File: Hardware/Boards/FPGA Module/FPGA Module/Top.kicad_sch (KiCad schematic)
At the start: 2 parts

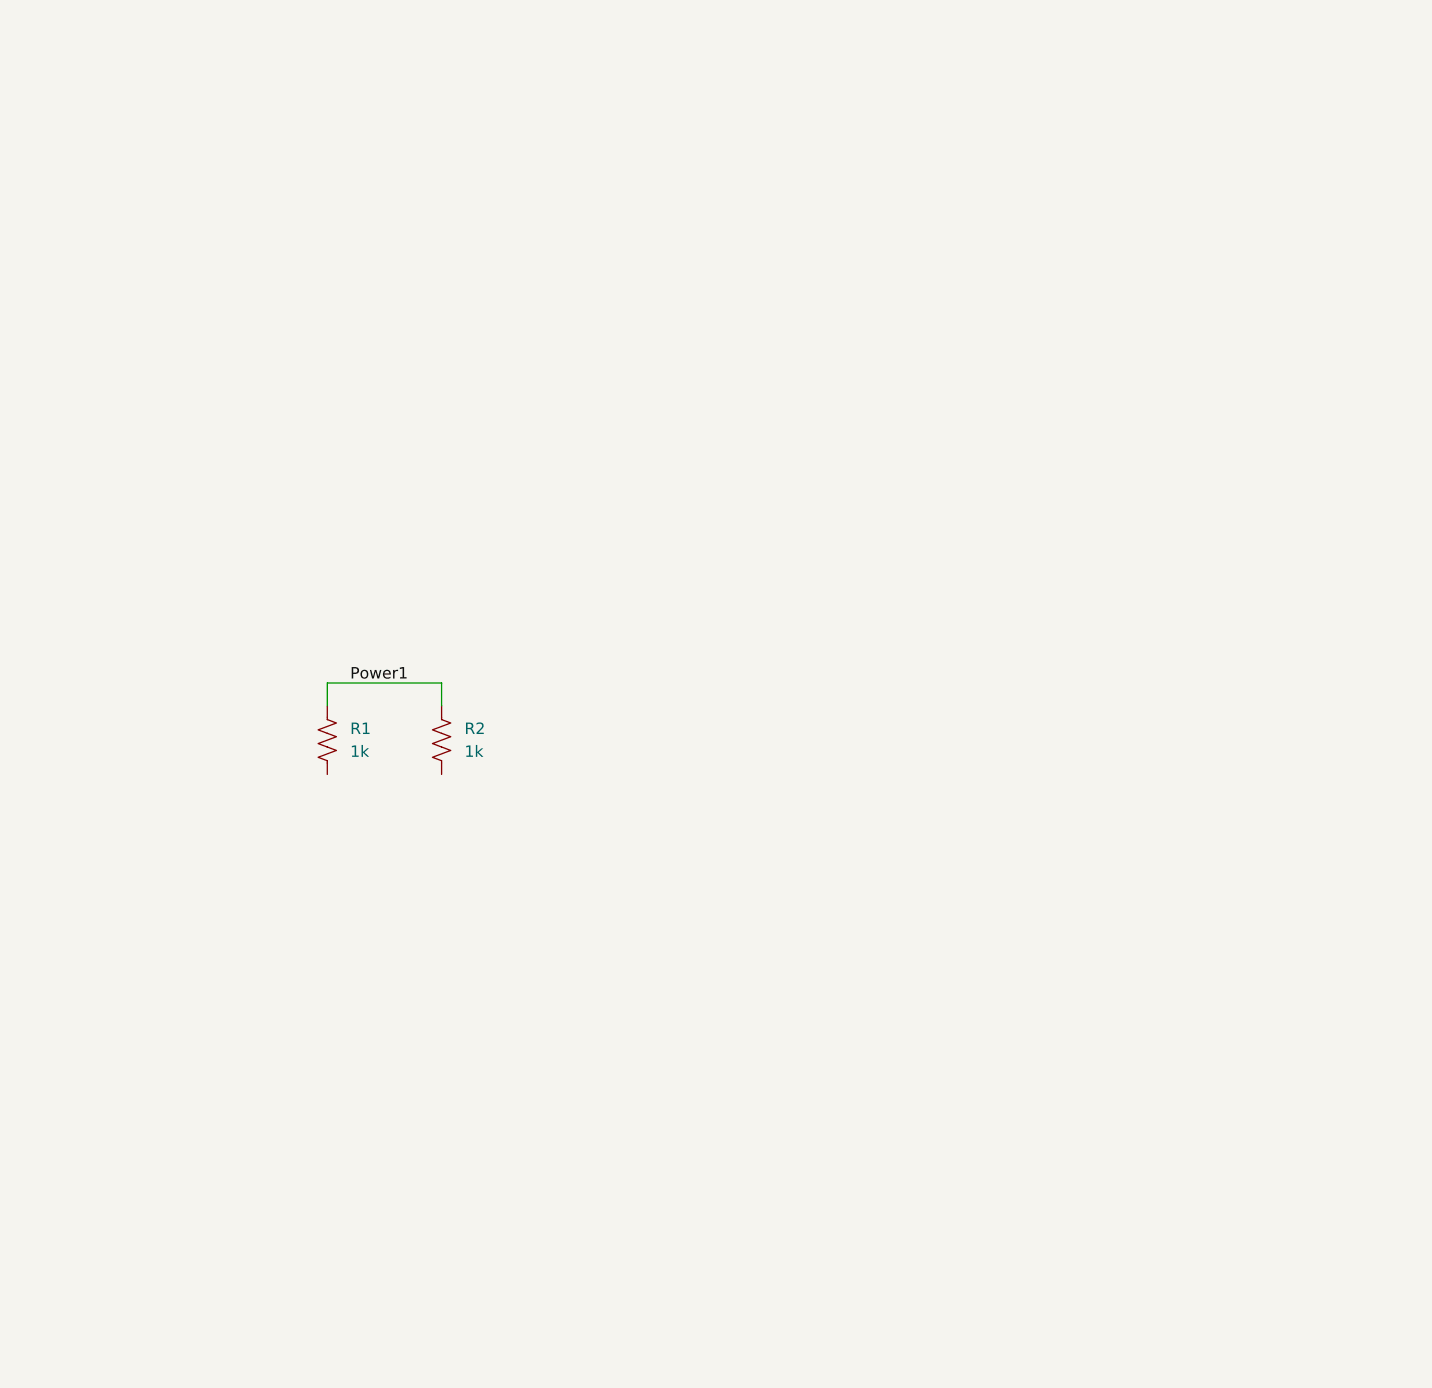
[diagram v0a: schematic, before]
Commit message: FPGA module schematic page creation
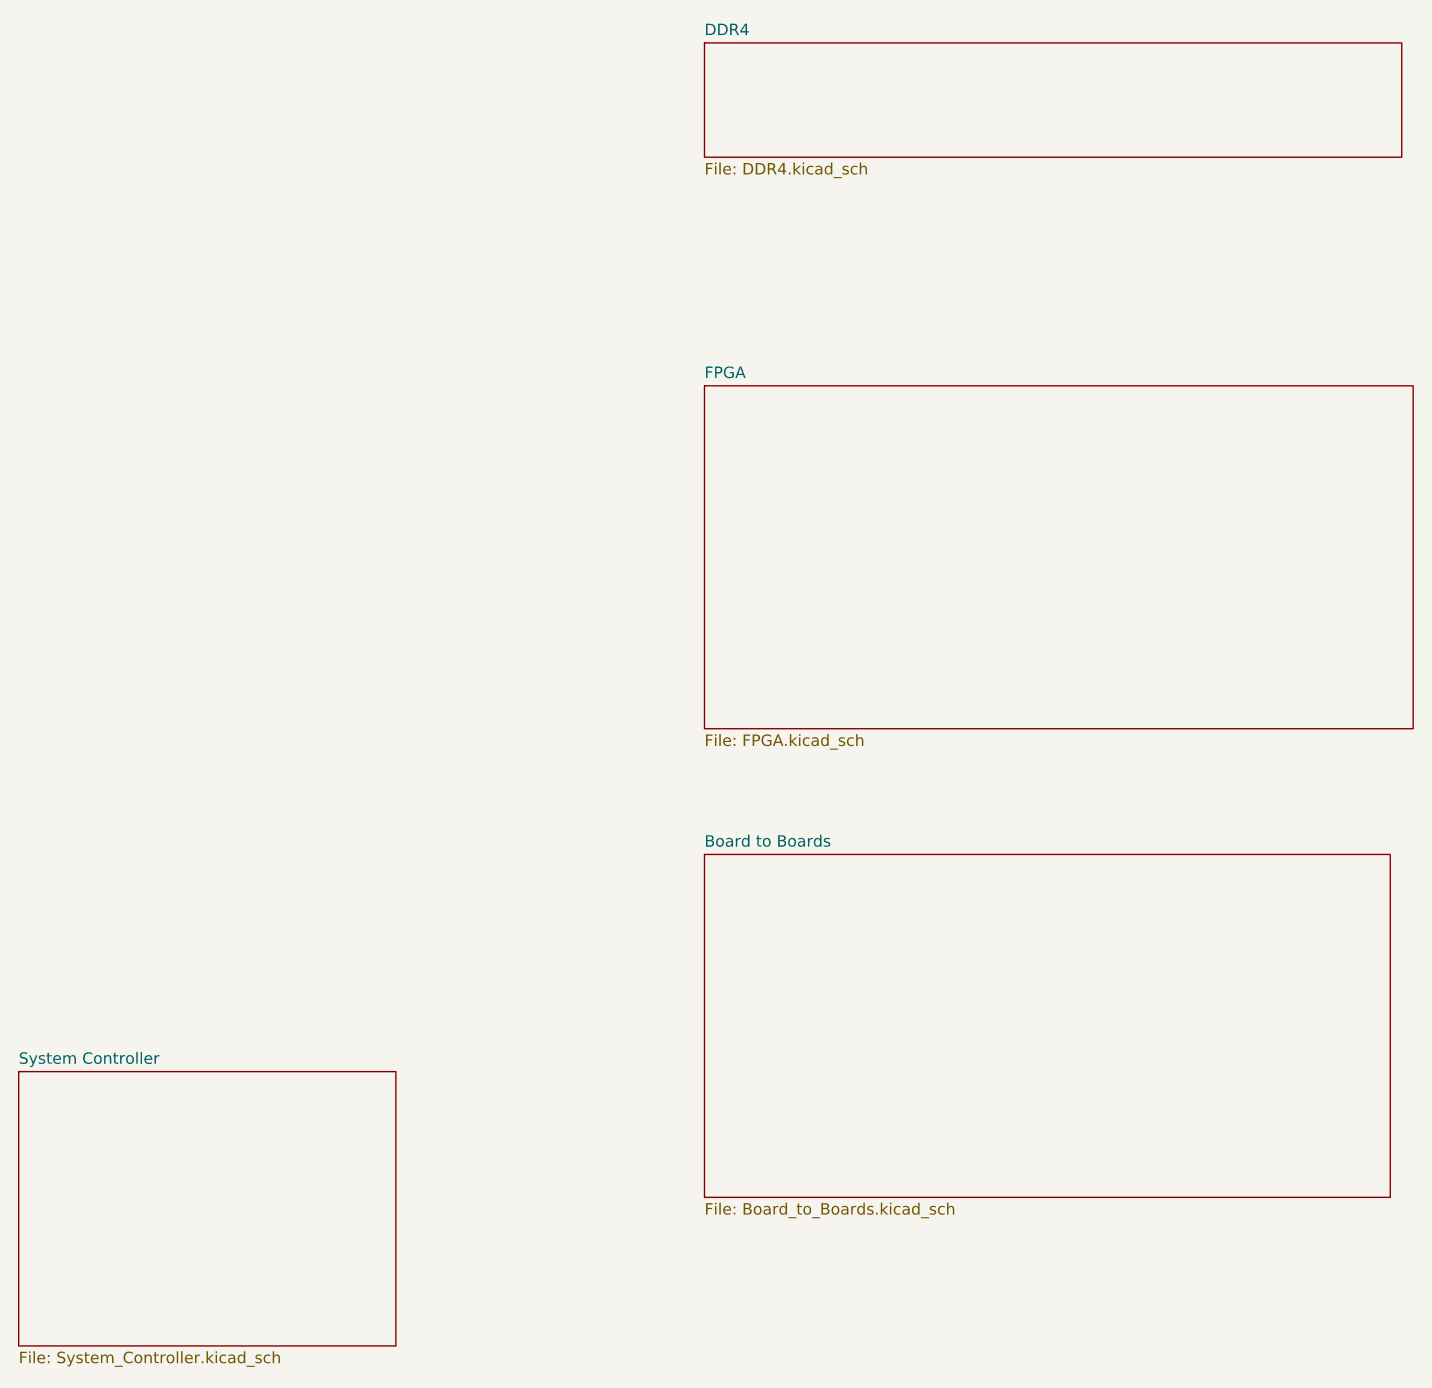
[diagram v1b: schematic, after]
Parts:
- removed R1, R2: 1k, Resistor_SMD:R_0402_1005Metric, symbol Device:R_US
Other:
- added sheet Board to Boards (Board_to_Boards.kicad_sch)
- added sheet DDR4 (DDR4.kicad_sch)
- added sheet FPGA (FPGA.kicad_sch)
- added sheet System Controller (System_Controller.kicad_sch)
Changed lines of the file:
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@@
 		(comment 1 "Designed by Michael Haahr")
 	)
-	(wire
-		(pts
-			(xy 123.19 96.52) (xy 123.19 99.06)
+	(sheet
+		(at 152.4 63.5)
+		(size 78.74 38.1)
+		(fields_autoplaced yes)
+		(stroke
+			(width 0.1524)
+			(type solid)
 		)
-		(stroke
-			(width 0)
-			(type default)
+		(fill
+			(color 0 0 0 0.0000)
 		)
-	)
-	(wire
-		(pts
-			(xy 110.49 99.06) (xy 110.49 96.52)
-		)
-		(stroke
-			(width 0)
-			(type default)
-		)
-	)
-	(wire
-		(pts
-			(xy 110.49 96.52) (xy 123.19 96.52)
-		)
-		(stroke
-			(width 0)
-			(type default)
-		)
-	)
-	(label "Power1"
-		(at 113.03 96.52 0)
-		(fields_autoplaced yes)
-		(effects
-			(font
-				(size 1.27 1.27)
-			)
-			(justify left bottom)
-		)
-	)
-	(symbol
-		(lib_id "Device:R_US")
-		(at 110.49 102.87 0)
-		(unit 1)
-		(exclude_from_sim no)
-		(in_bom yes)
-		(on_board yes)
-		(dnp no)
-		(fields_autoplaced yes)
-		(property "Reference" "R1"
-			(at 113.03 101.5999 0)
+		(property "Sheetname" "FPGA"
+			(at 152.4 62.7884 0)
 			(effects
 				(font
 					(size 1.27 1.27)
 				)
-				(justify left)
+				(justify left bottom)
 			)
 		)
-		(property "Value" "1k"
-			(at 113.03 104.1399 0)
+		(property "Sheetfile" "FPGA.kicad_sch"
+			(at 152.4 102.1846 0)
 			(effects
 				(font
 					(size 1.27 1.27)
 				)
-				(justify left)
+				(justify left top)
 			)
 		)
-		(property "Footprint" "Resistor_SMD:R_0402_1005Metric"
-			(at 111.506 103.124 90)
+		(instances
+			(project "FPGA Module"
+				(path "/199f10e2-d4b4-4a27-9e84-7b1ce2ae6bf0/0c296310-f788-47f0-8a3f-43c3444563e8"
+					(page "3")
+				)
+			)
+		)
+	)
+	(sheet
+		(at 152.4 25.4)
+		(size 77.47 12.7)
+		(fields_autoplaced yes)
+		(stroke
+			(width 0.1524)
+			(type solid)
+		)
+		(fill
+			(color 0 0 0 0.0000)
+		)
+		(property "Sheetname" "DDR4"
+			(at 152.4 24.6884 0)
 			(effects
 				(font
 					(size 1.27 1.27)
 				)
-				(hide yes)
+				(justify left bottom)
 			)
 		)
-		(property "Datasheet" "~"
-			(at 110.49 102.87 0)
+		(property "Sheetfile" "DDR4.kicad_sch"
+			(at 152.4 38.6846 0)
 			(effects
 				(font
 					(size 1.27 1.27)
 				)
-				(hide yes)
+				(justify left top)
 			)
 		)
-		(property "Description" "Resistor, US symbol"
-			(at 110.49 102.87 0)
+		(instances
+			(project "FPGA Module"
+				(path "/199f10e2-d4b4-4a27-9e84-7b1ce2ae6bf0/0c296310-f788-47f0-8a3f-43c3444563e8"
+					(page "4")
+				)
+			)
+		)
+	)
+	(sheet
+		(at 76.2 139.7)
+		(size 41.91 30.48)
+		(fields_autoplaced yes)
+		(stroke
+			(width 0.1524)
+			(type solid)
+		)
+		(fill
+			(color 0 0 0 0.0000)
+		)
+		(property "Sheetname" "System Controller"
+			(at 76.2 138.9884 0)
 			(effects
 				(font
 					(size 1.27 1.27)
 				)
-				(hide yes)
+				(justify left bottom)
 			)
 		)
-		(pin "2"
-		)
-		(pin "1"
+		(property "Sheetfile" "System_Controller.kicad_sch"
+			(at 76.2 170.7646 0)
+			(effects
+				(font
+					(size 1.27 1.27)
+				)
+				(justify left top)
+			)
 		)
 		(instances
-			(project ""
+			(project "FPGA Module"
 				(path "/199f10e2-d4b4-4a27-9e84-7b1ce2ae6bf0/0c296310-f788-47f0-8a3f-43c3444563e8"
-					(reference "R1")
-					(unit 1)
+					(page "5")
 				)
 			)
 		)
 	)
-	(symbol
-		(lib_id "Device:R_US")
-		(at 123.19 102.87 0)
-		(unit 1)
-		(exclude_from_sim no)
-		(in_bom yes)
-		(on_board yes)
-		(dnp no)
+	(sheet
+		(at 152.4 115.57)
+		(size 76.2 38.1)
 		(fields_autoplaced yes)
-		(property "Reference" "R2"
-			(at 125.73 101.5999 0)
+		(stroke
+			(width 0.1524)
+			(type solid)
+		)
+		(fill
+			(color 0 0 0 0.0000)
+		)
+		(property "Sheetname" "Board to Boards"
+			(at 152.4 114.8584 0)
 			(effects
 				(font
 					(size 1.27 1.27)
 				)
-				(justify left)
+				(justify left bottom)
 			)
 		)
-		(property "Value" "1k"
-			(at 125.73 104.1399 0)
+		(property "Sheetfile" "Board_to_Boards.kicad_sch"
+			(at 152.4 154.2546 0)
 			(effects
 				(font
 					(size 1.27 1.27)
 				)
-				(justify left)
+				(justify left top)
 			)
-		)
-		(property "Footprint" "Resistor_SMD:R_0402_1005Metric"
-			(at 124.206 103.124 90)
-			(effects
-				(font
-					(size 1.27 1.27)
-				)
-				(hide yes)
-			)
-		)
-		(property "Datasheet" "~"
-			(at 123.19 102.87 0)
-			(effects
-				(font
-					(size 1.27 1.27)
-				)
-				(hide yes)
-			)
-		)
-		(property "Description" "Resistor, US symbol"
-			(at 123.19 102.87 0)
-			(effects
-				(font
-					(size 1.27 1.27)
-				)
-				(hide yes)
-			)
-		)
-		(pin "2"
-		)
-		(pin "1"
 		)
 		(instances
 			(project "FPGA Module"
 				(path "/199f10e2-d4b4-4a27-9e84-7b1ce2ae6bf0/0c296310-f788-47f0-8a3f-43c3444563e8"
-					(reference "R2")
-					(unit 1)
+					(page "6")
 				)
 			)

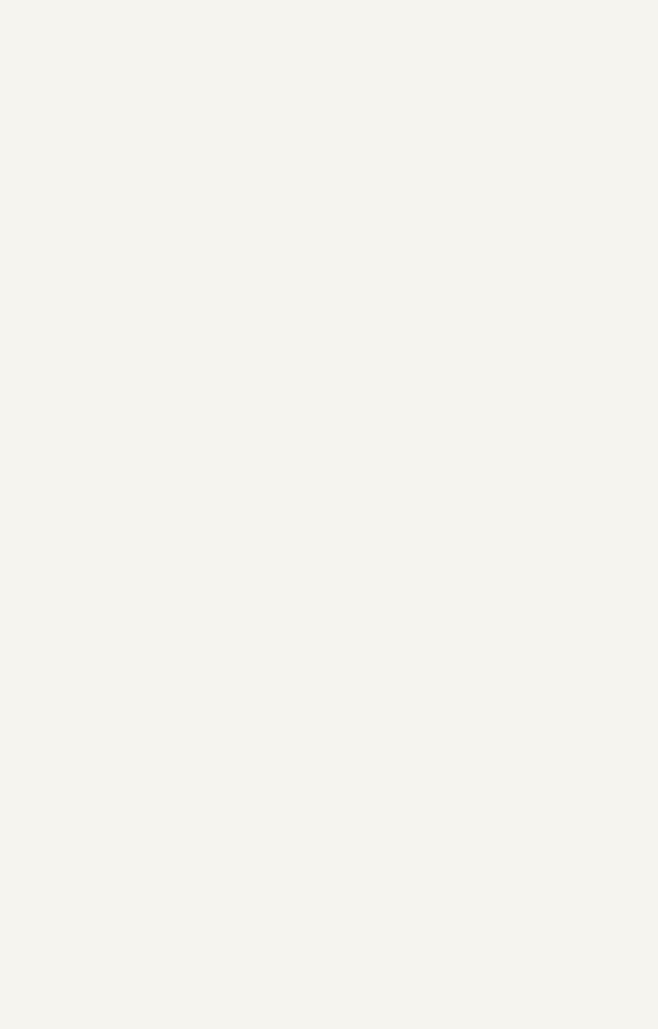
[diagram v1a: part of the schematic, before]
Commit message: More schematic pages for FPGA module
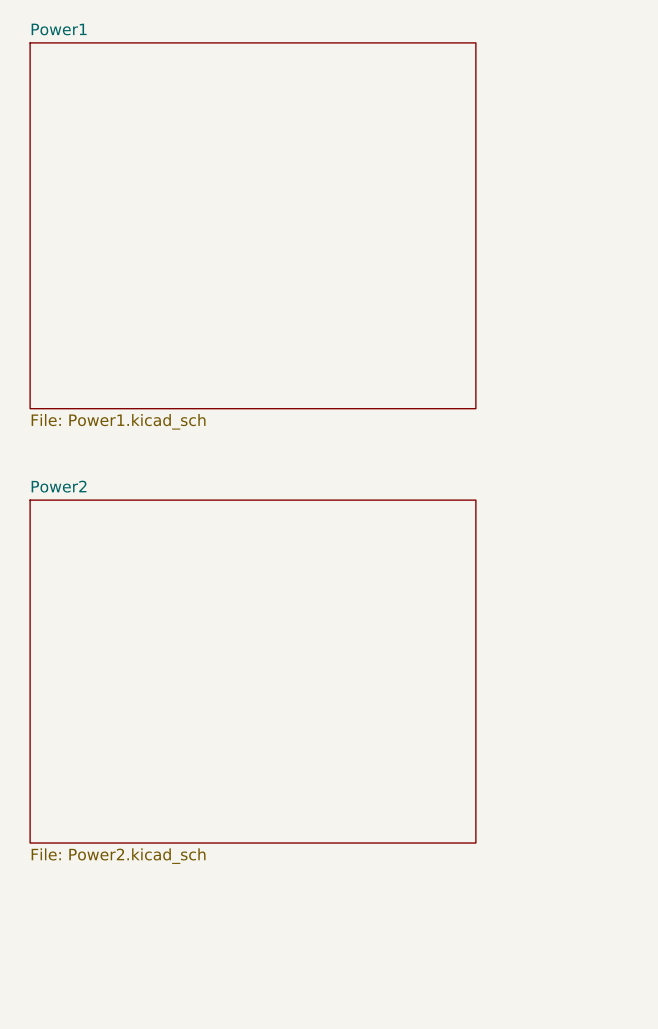
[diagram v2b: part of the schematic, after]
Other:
- added sheet Power1 (Power1.kicad_sch)
- added sheet Power2 (Power2.kicad_sch)
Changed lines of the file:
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@@
+	)
+	(sheet
+		(at 77.47 76.2)
+		(size 49.53 38.1)
+		(fields_autoplaced yes)
+		(stroke
+			(width 0.1524)
+			(type solid)
+		)
+		(fill
+			(color 0 0 0 0.0000)
+		)
+		(property "Sheetname" "Power2"
+			(at 77.47 75.4884 0)
+			(effects
+				(font
+					(size 1.27 1.27)
+				)
+				(justify left bottom)
+			)
+		)
+		(property "Sheetfile" "Power2.kicad_sch"
+			(at 77.47 114.8846 0)
+			(effects
+				(font
+					(size 1.27 1.27)
+				)
+				(justify left top)
+			)
+		)
+		(instances
+			(project "FPGA Module"
+				(path "/199f10e2-d4b4-4a27-9e84-7b1ce2ae6bf0/0c296310-f788-47f0-8a3f-43c3444563e8"
+					(page "8")
+				)
+			)
+		)
 	)
 	(sheet
@@
 				)
 			)
+		)
+	)
+	(sheet
+		(at 77.47 25.4)
+		(size 49.53 40.64)
+		(fields_autoplaced yes)
+		(stroke
+			(width 0.1524)
+			(type solid)
+		)
+		(fill
+			(color 0 0 0 0.0000)
+		)
+		(property "Sheetname" "Power1"
+			(at 77.47 24.6884 0)
+			(effects
+				(font
+					(size 1.27 1.27)
+				)
+				(justify left bottom)
+			)
+		)
+		(property "Sheetfile" "Power1.kicad_sch"
+			(at 77.47 66.6246 0)
+			(effects
+				(font
+					(size 1.27 1.27)
+				)
+				(justify left top)
+			)
+		)
+		(instances
+			(project "FPGA Module"
+				(path "/199f10e2-d4b4-4a27-9e84-7b1ce2ae6bf0/0c296310-f788-47f0-8a3f-43c3444563e8"
+					(page "7")
+				)
+			)
